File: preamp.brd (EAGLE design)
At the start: 127 x 76.2 mm, 30 parts, among them IC1 INA2141U, IC2 INA2141U, IC3 INA2141U

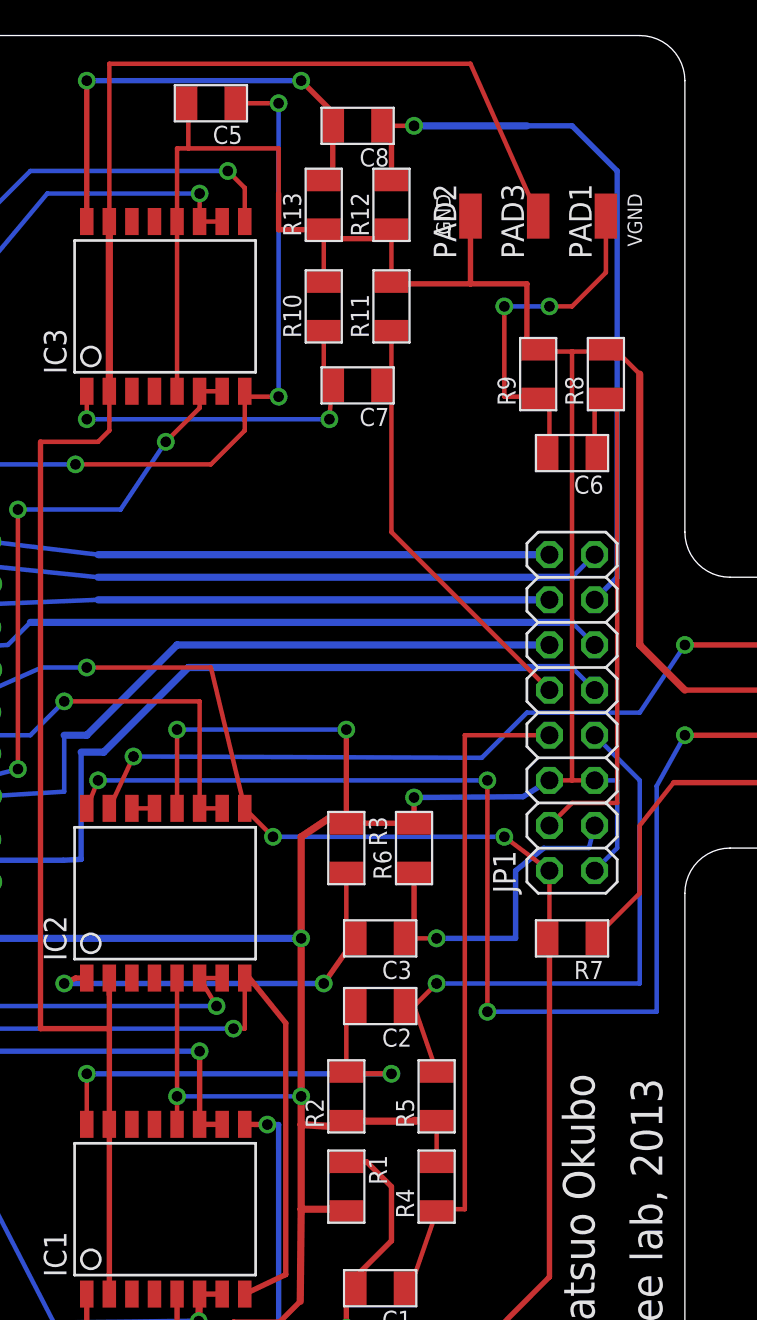
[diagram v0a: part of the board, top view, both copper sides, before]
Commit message: Preamp - Removed VGROUND
SIGNAL_GROUND net changed to GROUND
Removed filter circuitry for VGROUND
Removed toggle switch between GROUND and FILTERED_VGND for
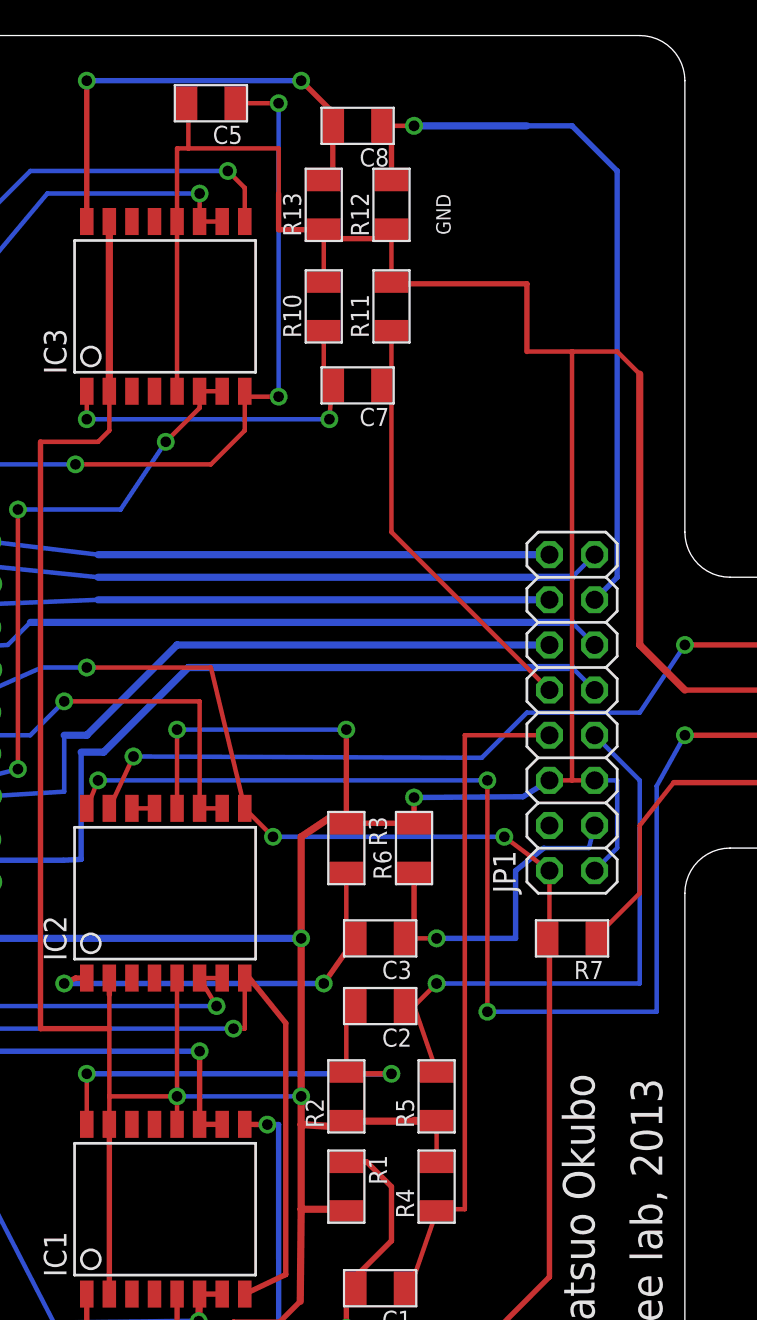
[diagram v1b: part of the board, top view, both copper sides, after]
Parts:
- removed C6: 47nF, elm:R0805ELM
- removed PAD1, PAD2, PAD3: (no value), wirepad:SMD1,27-2,54
- removed R8: 22k, elm:R0805ELM
- removed R9: 1.5M, elm:R0805ELM
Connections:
- removed net FILTERED_VGROUND: C6.2, PAD1.1, R9.1
- removed net SIGNAL_GROUND: IC1.15, IC1.2, IC2.2, IC3.15, IC3.2, PAD3.1
- net GROUND: now also IC1.15, IC1.2, IC2.2, IC3.15, IC3.2; no longer PAD2.1, R8.2, R9.2
- net VGROUND: no longer C6.1, R8.1
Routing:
- net SIGNAL_GROUND: track 110.1 -> 0.00 mm
- net GROUND: track 312.1 -> 382.2 mm
- net VGROUND: track 31.7 -> 0.00 mm
- net FILTERED_VGROUND: track 21.1 -> 0.00 mm, vias 2 -> 0
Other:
- board text removed: "VGND"

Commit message: Changed JP1 pinout to match drive
Stim 1 In > DGND
Stim 1 Out > SCL
IX > IX
E4 > SDA
VGND > E3
E5 > E1
E3 > E4
GROUND > E2
E2 > ICOM
ICOM > V+
E1 > GROUND
V+ > V-
STIM2 stays the same
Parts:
- moved R7 14.5 mm to (55.9, 34.3)
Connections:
- net STIM1OUT renamed SCL
- removed net STIM1IN: JP1.16, U$3._D
- removed net VGROUND: JP1.4
- new net DGND: JP1.16, U$3._C
- new net SDA: JP1.10, U$3._D
- net CHAN1: now also IC3.6, IC3.7; no longer IC1.6, IC1.7
- net CHAN4: now also IC1.6, IC1.7; no longer IC3.6, IC3.7
- net E1: now also C7.1, JP1.13, R11.1; no longer C1.1, JP1.8, R4.1
- net E2: now also JP1.1, JP1.5, JP1.6; no longer JP1.7
- net E3: now also JP1.4; no longer JP1.3
- net E4: now also C1.1, JP1.3, R4.1; no longer C7.1, JP1.10, R11.1
- net E5: no longer JP1.13
- net GROUND: now also JP1.8; no longer JP1.1, JP1.5, JP1.6
- net ICOM: now also JP1.7; no longer JP1.12
- net V+: now also JP1.12; no longer JP1.2
- net V-: now also JP1.2
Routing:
- net DGND: track 0.00 -> 37.2 mm
- net SDA: track 0.00 -> 35.0 mm, vias 0 -> 2
- net STIM1IN: track 31.5 -> 0.00 mm
- net CHAN1: track 56.6 -> 26.6 mm
- net GROUND: track 382.2 -> 352.5 mm
- net V+: track 148.6 -> 121.2 mm, vias 8 -> 5
- net V+_HALL: track 84.6 -> 67.0 mm
- net E4: track 24.7 -> 39.5 mm
- net V-: track 116.0 -> 127.7 mm, vias 6 -> 5
- net E1: track 37.9 -> 27.8 mm
- net E3: track 19.6 -> 12.6 mm
- net CHAN4: track 34.9 -> 40.8 mm
- net V-_INC: track 23.4 -> 27.4 mm
- net E5: track 42.0 -> 40.2 mm
- net ICOM: track 36.7 -> 38.1 mm, vias 0 -> 3
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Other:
- board text removed: "GND"
